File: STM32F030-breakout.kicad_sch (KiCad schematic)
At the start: 37 parts, among them J1 Conn_01x24, J2 Conn_01x24, J5 TagConnect_TC2030, J6 USB_C_Receptacle_USB2.0, U1 STM32F030C8Tx, U2 MCP1802x-xx02xOT, U3 LP5907MFX-3.3, X1 ASE-xxxMHz, Y1 Crystal

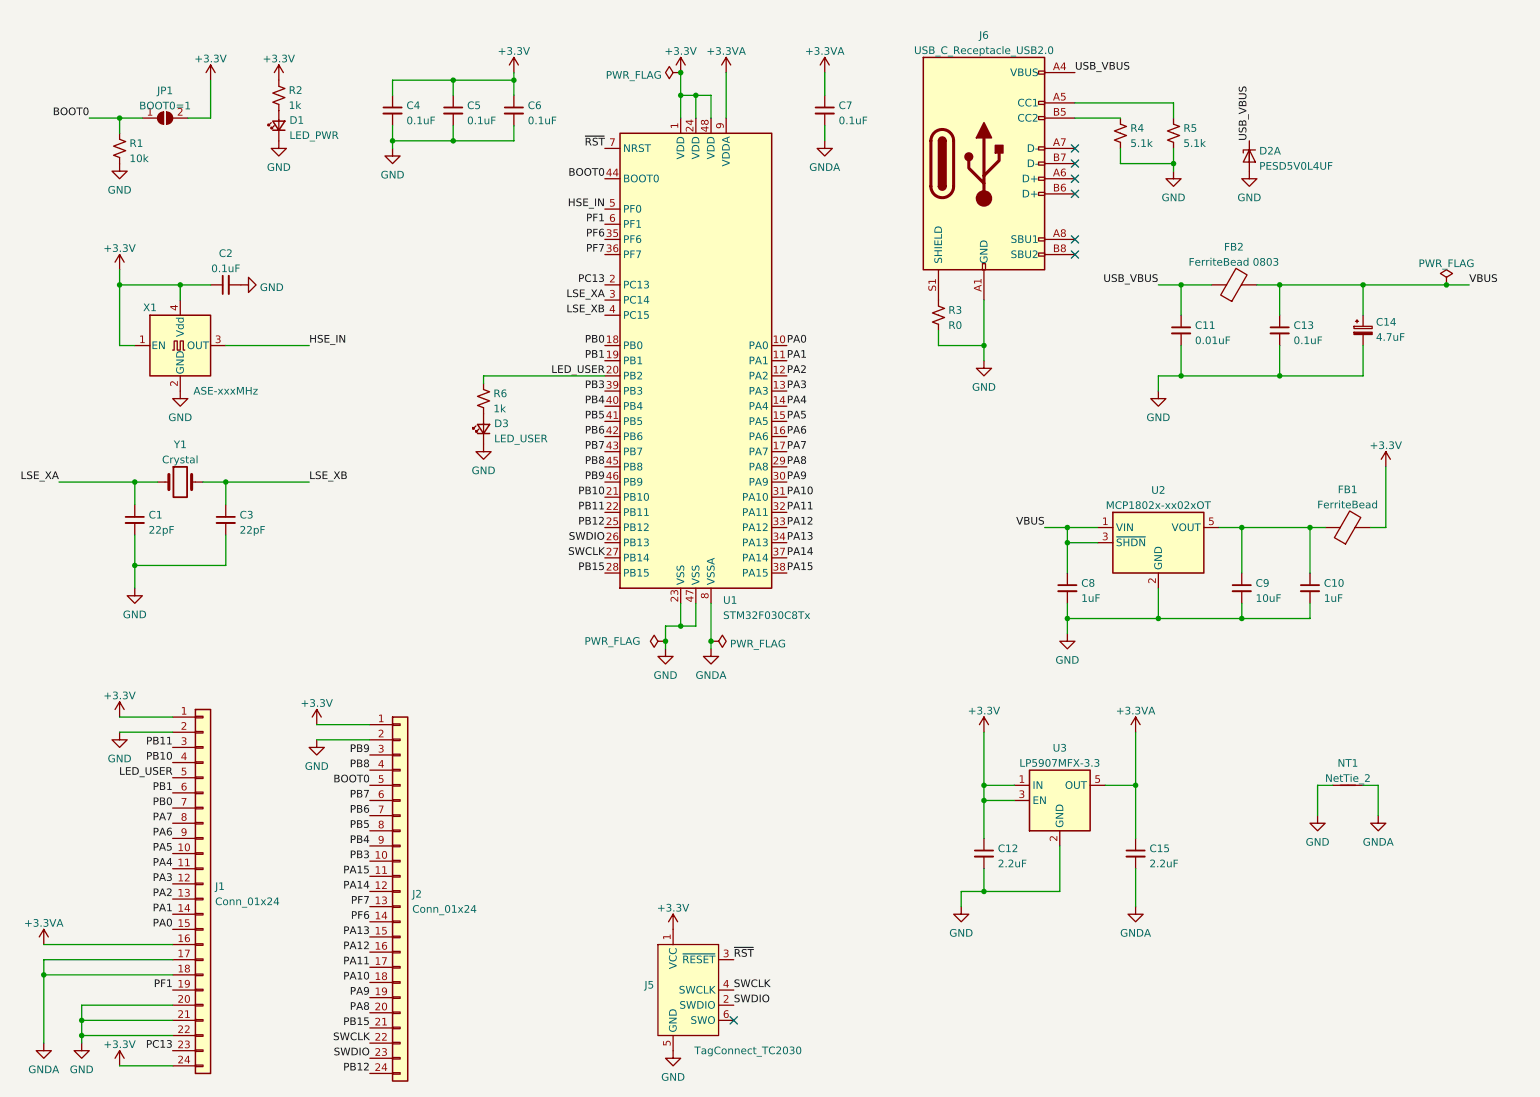
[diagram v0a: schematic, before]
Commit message: Revision v1: 4-layer board; reset button
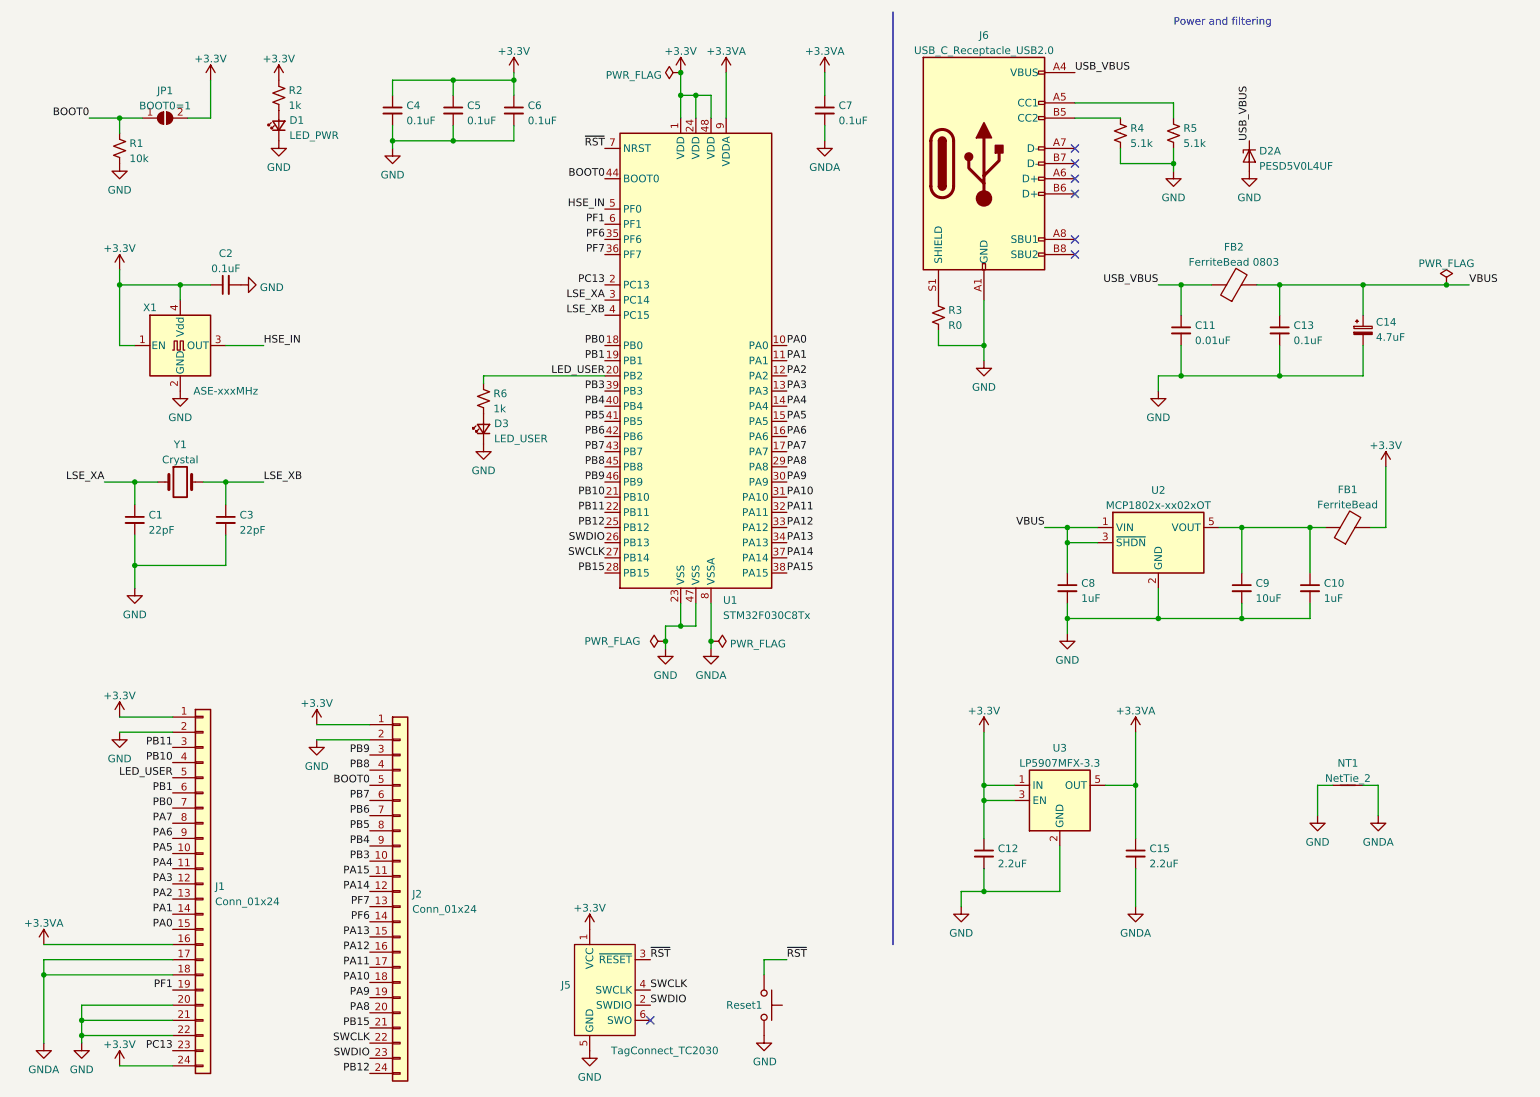
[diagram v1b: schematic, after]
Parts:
- added Reset1: SW_Push, Button_Switch_SMD:SW_SPST_B3U-1000P-B, symbol Switch:SW_Push
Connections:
- net GND: now also Reset1.2
- net ~{RST}: now also Reset1.1
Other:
- note added: "Power and filtering"
- moved on the sheet: J5

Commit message: Oof. SWDIO and SWCLK were on the wrong bank.
I made the mistake of swapping out a different F030 symbol in Kicad. Turns out
the A and B ports were swapped!
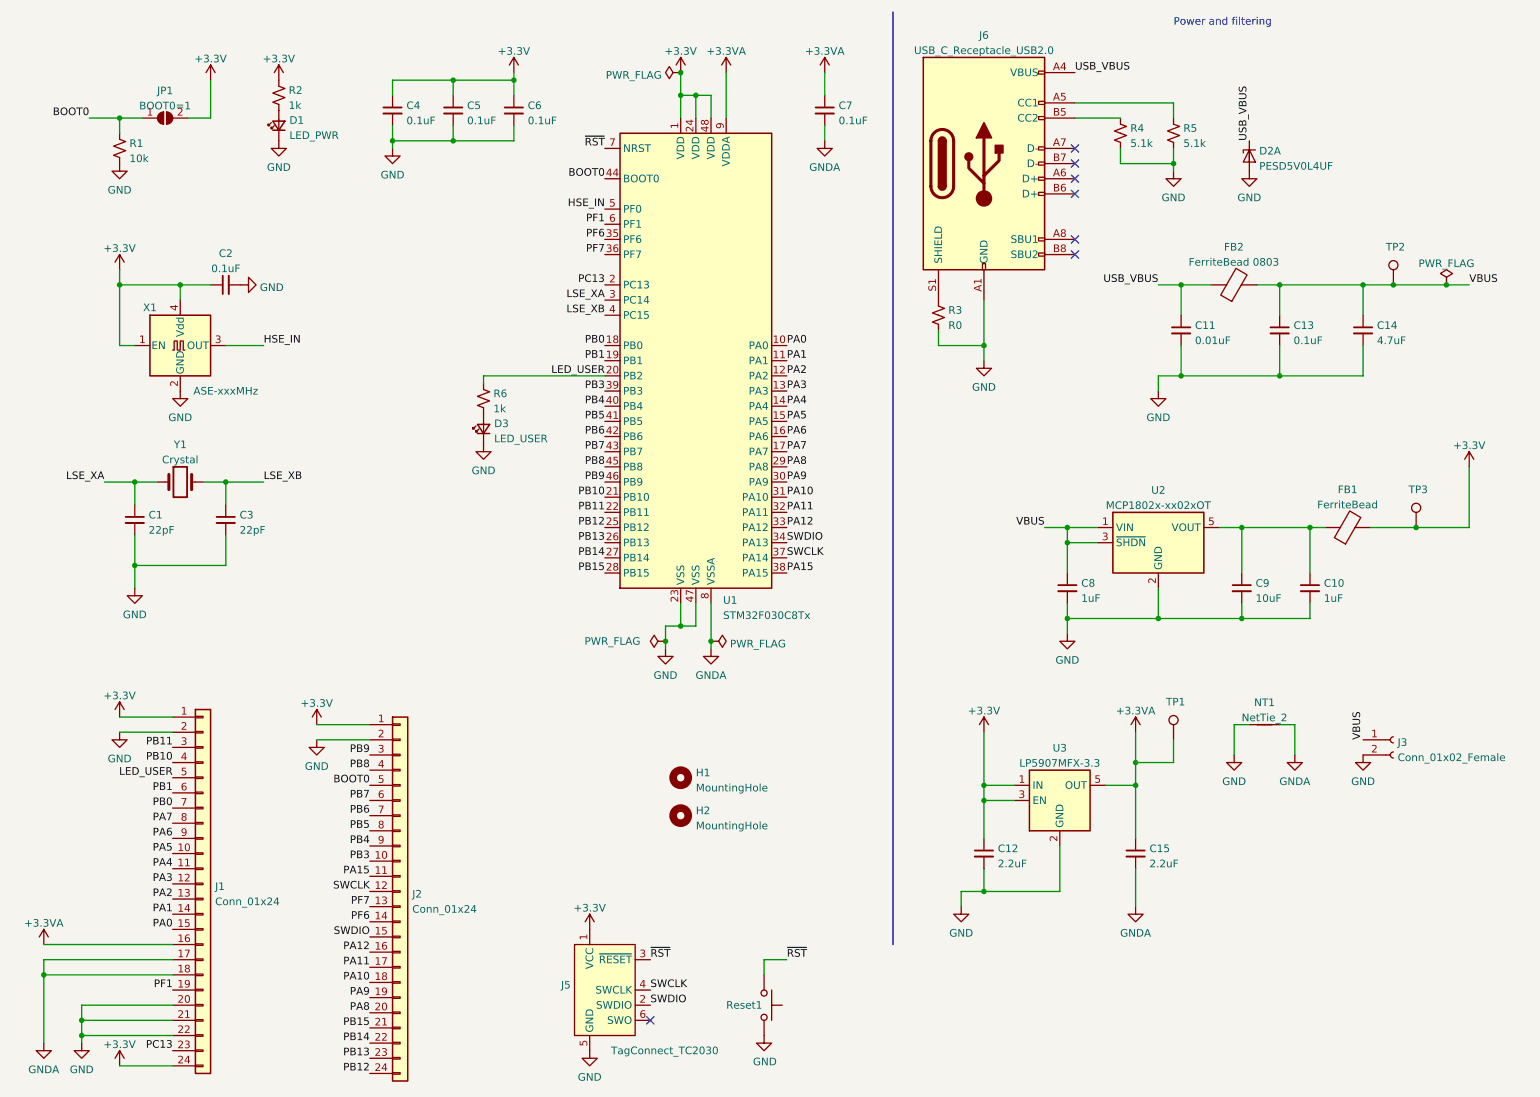
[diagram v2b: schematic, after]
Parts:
- removed C14: 4.7uF, Capacitor_SMD:CP_Elec_5x3, symbol Device:C_Polarized_Small
- added C14: 4.7uF, Capacitor_SMD:C_0805_2012Metric, symbol Device:C_Small
- added H1, H2: MountingHole, MountingHole:MountingHole_2.2mm_M2, symbol Mechanical:MountingHole
- added J3: Conn_01x02_Female, Connector_PinHeader_2.54mm:PinHeader_1x02_P2.54mm_Vertical, symbol Connector:Conn_01x02_Female
- added TP1, TP2, TP3: TestPoint, TestPoint:TestPoint_Pad_D1.0mm, symbol Connector:TestPoint
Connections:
- net PA13 is gone; now on net SWDIO: J2.15 (Pin_15), U1.34 (PA13)
- net PA14 is gone; now on net SWCLK: J2.12 (Pin_12), U1.37 (PA14)
- net +3.3V: now also TP3.1
- net +3.3VA: now also TP1.1
- net GND: now also C14.2, J3.2 (Pin_2)
- net SWCLK: no longer J2.22 (Pin_22), U1.27 (PB14)
- net SWDIO: no longer J2.23 (Pin_23), U1.26 (PB13)
- net VBUS: now also C14.1, J3.1 (Pin_1), TP2.1
- new net PB13: J2.23 (Pin_23), U1.26 (PB13)
- new net PB14: J2.22 (Pin_22), U1.27 (PB14)
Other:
- moved on the sheet: NT1
